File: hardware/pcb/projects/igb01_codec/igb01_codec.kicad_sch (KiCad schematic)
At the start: 46 parts, among them J1 Conn_01x08, J2 Conn_01x08, U1 AK4619

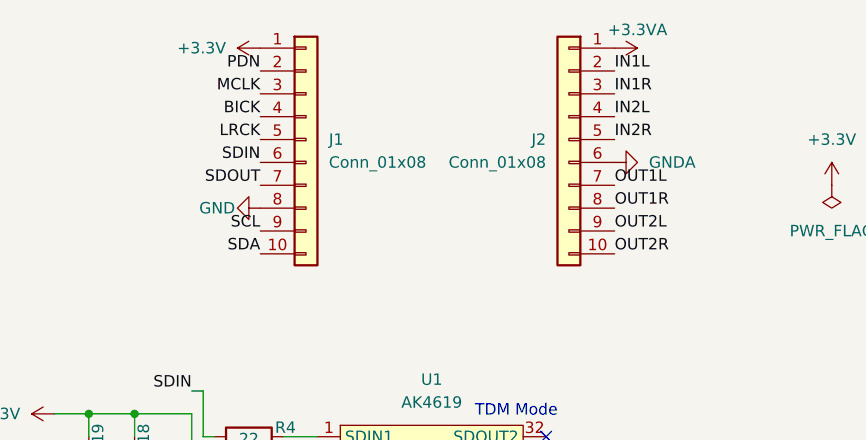
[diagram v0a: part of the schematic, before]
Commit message: add control pcb schematic
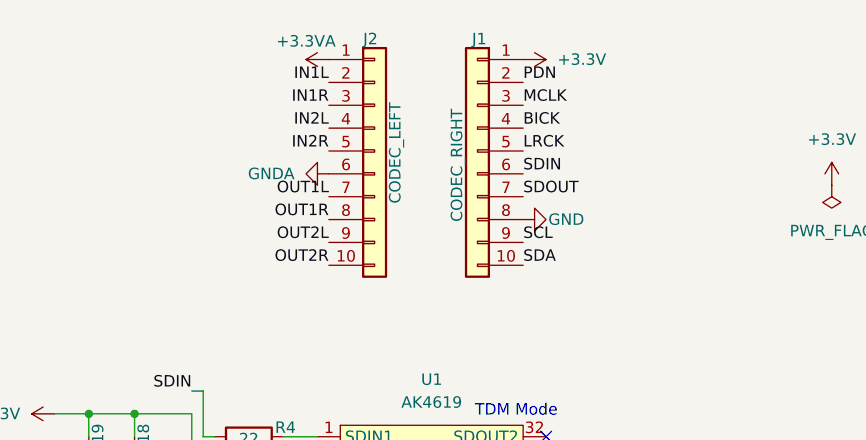
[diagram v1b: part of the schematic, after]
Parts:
- J1: value Conn_01x08 -> CODEC_RIGHT
- J2: value Conn_01x08 -> CODEC_LEFT
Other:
- moved on the sheet: J1, J2
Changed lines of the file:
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@@
 	)
 	(label "SDOUT"
-		(at 124.46 39.37 180)
+		(at 153.67 40.64 0)
 		(effects
 			(font
 				(size 1.27 1.27)
 			)
-			(justify right bottom)
+			(justify left bottom)
 		)
 	)
@@
 	)
 	(label "IN1L"
-		(at 163.83 26.67 0)
+		(at 132.08 27.94 180)
 		(effects
 			(font
 				(size 1.27 1.27)
 			)
-			(justify left bottom)
+			(justify right bottom)
 		)
 	)
@@
 	)
 	(label "OUT1R"
-		(at 163.83 41.91 0)
+		(at 132.08 43.18 180)
 		(effects
 			(font
 				(size 1.27 1.27)
 			)
-			(justify left bottom)
+			(justify right bottom)
 		)
 	)
 	(label "OUT2R"
-		(at 163.83 46.99 0)
+		(at 132.08 48.26 180)
 		(effects
 			(font
 				(size 1.27 1.27)
 			)
-			(justify left bottom)
+			(justify right bottom)
 		)
 	)
 	(label "OUT2L"
-		(at 163.83 44.45 0)
+		(at 132.08 45.72 180)
 		(effects
 			(font
 				(size 1.27 1.27)
 			)
-			(justify left bottom)
+			(justify right bottom)
 		)
 	)
@@
 	)
 	(label "LRCK"
-		(at 124.46 34.29 180)
+		(at 153.67 35.56 0)
 		(effects
 			(font
 				(size 1.27 1.27)
 			)
-			(justify right bottom)
+			(justify left bottom)
 		)
 	)
 	(label "OUT1L"
-		(at 163.83 39.37 0)
+		(at 132.08 40.64 180)
 		(effects
 			(font
 				(size 1.27 1.27)
 			)
-			(justify left bottom)
+			(justify right bottom)
 		)
 	)
@@
 	)
 	(label "SDA"
-		(at 124.46 46.99 180)
+		(at 153.67 48.26 0)
 		(effects
 			(font
 				(size 1.27 1.27)
 			)
-			(justify right bottom)
+			(justify left bottom)
 		)
 	)
 	(label "IN1R"
-		(at 163.83 29.21 0)
+		(at 132.08 30.48 180)
 		(effects
 			(font
 				(size 1.27 1.27)
 			)
-			(justify left bottom)
+			(justify right bottom)
 		)
 	)
 	(label "SDIN"
-		(at 124.46 36.83 180)
+		(at 153.67 38.1 0)
 		(effects
 			(font
 				(size 1.27 1.27)
 			)
-			(justify right bottom)
+			(justify left bottom)
 		)
 	)
 	(label "BICK"
-		(at 124.46 31.75 180)
+		(at 153.67 33.02 0)
 		(effects
 			(font
 				(size 1.27 1.27)
 			)
-			(justify right bottom)
+			(justify left bottom)
 		)
 	)
@@
 	)
 	(label "MCLK"
-		(at 124.46 29.21 180)
+		(at 153.67 30.48 0)
 		(effects
 			(font
 				(size 1.27 1.27)
 			)
-			(justify right bottom)
+			(justify left bottom)
 		)
 	)
@@
 	)
 	(label "IN2L"
-		(at 163.83 31.75 0)
+		(at 132.08 33.02 180)
 		(effects
 			(font
 				(size 1.27 1.27)
 			)
-			(justify left bottom)
+			(justify right bottom)
 		)
 	)
@@
 	)
 	(label "PDN"
-		(at 124.46 26.67 180)
+		(at 153.67 27.94 0)
 		(effects
 			(font
 				(size 1.27 1.27)
 			)
-			(justify right bottom)
+			(justify left bottom)
 		)
 	)
 	(label "IN2R"
-		(at 163.83 34.29 0)
+		(at 132.08 35.56 180)
 		(effects
 			(font
 				(size 1.27 1.27)
 			)
-			(justify left bottom)
+			(justify right bottom)
 		)
 	)
 	(label "SCL"
-		(at 124.46 44.45 180)
+		(at 153.67 45.72 0)
 		(effects
 			(font
 				(size 1.27 1.27)
 			)
-			(justify right bottom)
+			(justify left bottom)
 		)
 	)
@@
 	(symbol
 		(lib_id "power:GNDA")
-		(at 163.83 36.83 90)
+		(at 132.08 38.1 270)
+		(mirror x)
 		(unit 1)
 		(exclude_from_sim no)
@@
 		(fields_autoplaced yes)
 		(property "Reference" "#PWR019"
-			(at 170.18 36.83 0)
+			(at 125.73 38.1 0)
 			(effects
 				(font
@@
 		)
 		(property "Value" "GNDA"
-			(at 167.64 36.8299 90)
+			(at 128.27 38.0999 90)
 			(effects
 				(font
@@
 		)
 		(property "Footprint" ""
-			(at 163.83 36.83 0)
+			(at 132.08 38.1 0)
 			(effects
 				(font
@@
 		)
 		(property "Datasheet" ""
-			(at 163.83 36.83 0)
+			(at 132.08 38.1 0)
 			(effects
 				(font
@@
 		)
 		(property "Description" "Power symbol creates a global label with name \"GNDA\" , analog ground"
-			(at 163.83 36.83 0)
+			(at 132.08 38.1 0)
 			(effects
 				(font
@@
 	(symbol
 		(lib_id "Connector_Generic:Conn_01x10")
-		(at 158.75 34.29 0)
-		(mirror y)
+		(at 137.16 35.56 0)
 		(unit 1)
 		(exclude_from_sim no)
@@
 		(dnp no)
 		(property "Reference" "J2"
-			(at 156.21 34.2899 0)
+			(at 135.89 23.114 0)
 			(effects
 				(font
@@
 			)
 		)
-		(property "Value" "Conn_01x08"
-			(at 156.21 36.8299 0)
+		(property "Value" "CODEC_LEFT"
+			(at 139.446 41.402 90)
 			(effects
 				(font
@@
 		)
 		(property "Footprint" ""
-			(at 158.75 34.29 0)
+			(at 137.16 35.56 0)
 			(effects
 				(font
@@
 		)
 		(property "Datasheet" "~"
-			(at 158.75 34.29 0)
+			(at 137.16 35.56 0)
 			(effects
 				(font
@@
 		)
 		(property "Description" "Generic connector, single row, 01x10, script generated (kicad-library-utils/schlib/autogen/connector/)"
-			(at 158.75 34.29 0)
+			(at 137.16 35.56 0)
 			(effects
 				(font
@@
 	(symbol
 		(lib_id "power:+3.3V")
-		(at 124.46 24.13 90)
+		(at 153.67 25.4 270)
+		(mirror x)
 		(unit 1)
 		(exclude_from_sim no)
@@
 		(fields_autoplaced yes)
 		(property "Reference" "#PWR016"
-			(at 128.27 24.13 0)
+			(at 149.86 25.4 0)
 			(effects
 				(font
@@
 		)
 		(property "Value" "+3.3V"
-			(at 120.65 24.1299 90)
+			(at 157.48 25.3999 90)
 			(effects
 				(font
@@
 		)
 		(property "Footprint" ""
-			(at 124.46 24.13 0)
+			(at 153.67 25.4 0)
 			(effects
 				(font
@@
 		)
 		(property "Datasheet" ""
-			(at 124.46 24.13 0)
+			(at 153.67 25.4 0)
 			(effects
 				(font
@@
 		)
 		(property "Description" "Power symbol creates a global label with name \"+3.3V\""
-			(at 124.46 24.13 0)
+			(at 153.67 25.4 0)
 			(effects
 				(font
@@
 	(symbol
 		(lib_id "power:GND")
-		(at 124.46 41.91 270)
+		(at 153.67 43.18 90)
+		(mirror x)
 		(unit 1)
 		(exclude_from_sim no)
@@
 		(dnp no)
 		(property "Reference" "#PWR017"
-			(at 118.11 41.91 0)
+			(at 160.02 43.18 0)
 			(effects
 				(font
@@
 		)
 		(property "Value" "GND"
-			(at 121.666 41.91 90)
+			(at 156.464 43.18 90)
 			(effects
 				(font
@@
 		)
 		(property "Footprint" ""
-			(at 124.46 41.91 0)
+			(at 153.67 43.18 0)
 			(effects
 				(font
@@
 		)
 		(property "Datasheet" ""
-			(at 124.46 41.91 0)
+			(at 153.67 43.18 0)
 			(effects
 				(font
@@
 		)
 		(property "Description" "Power symbol creates a global label with name \"GND\" , ground"
-			(at 124.46 41.91 0)
+			(at 153.67 43.18 0)
 			(effects
 				(font
@@
 	(symbol
 		(lib_id "Connector_Generic:Conn_01x10")
-		(at 129.54 34.29 0)
+		(at 148.59 35.56 0)
+		(mirror y)
 		(unit 1)
 		(exclude_from_sim no)
@@
 		(on_board yes)
 		(dnp no)
-		(fields_autoplaced yes)
 		(property "Reference" "J1"
-			(at 132.08 34.2899 0)
+			(at 149.606 23.114 0)
 			(effects
 				(font
@@
 			)
 		)
-		(property "Value" "Conn_01x08"
-			(at 132.08 36.8299 0)
+		(property "Value" "CODEC_RIGHT"
+			(at 146.304 43.434 90)
 			(effects
 				(font
@@
 		)
 		(property "Footprint" ""
-			(at 129.54 34.29 0)
+			(at 148.59 35.56 0)
 			(effects
 				(font
@@
 		)
 		(property "Datasheet" "~"
-			(at 129.54 34.29 0)
+			(at 148.59 35.56 0)
 			(effects
 				(font
@@
 		)
 		(property "Description" "Generic connector, single row, 01x10, script generated (kicad-library-utils/schlib/autogen/connector/)"
-			(at 129.54 34.29 0)
+			(at 148.59 35.56 0)
 			(effects
 				(font
@@
 	(symbol
 		(lib_id "power:+3.3VA")
-		(at 163.83 24.13 270)
+		(at 132.08 25.4 90)
+		(mirror x)
 		(unit 1)
 		(exclude_from_sim no)
@@
 		(dnp no)
 		(property "Reference" "#PWR018"
-			(at 160.02 24.13 0)
+			(at 135.89 25.4 0)
 			(effects
 				(font
@@
 		)
 		(property "Value" "+3.3VA"
-			(at 163.068 22.098 90)
+			(at 132.842 23.368 90)
 			(effects
 				(font
@@
 		)
 		(property "Footprint" ""
-			(at 163.83 24.13 0)
+			(at 132.08 25.4 0)
 			(effects
 				(font
@@
 		)
 		(property "Datasheet" ""
-			(at 163.83 24.13 0)
+			(at 132.08 25.4 0)
 			(effects
 				(font
@@
 		)
 		(property "Description" "Power symbol creates a global label with name \"+3.3VA\""
-			(at 163.83 24.13 0)
+			(at 132.08 25.4 0)
 			(effects
 				(font

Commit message: update codec sch&pcb
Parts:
- removed C10, C12, C14, C16: 1u_DIP, symbol Device:C_Small
- removed C11, C13, C15, C9: 1u_SMD, symbol Device:C_Small
- removed JP1: SolderJumper_2_Open, symbol Jumper:SolderJumper_2_Open
- C1, C3, C5, C7: footprint (none) -> Capacitor_SMD:C_1206_3216Metric
- C10: renamed from C18; footprint (none) -> Capacitor_SMD:C_0402_1005Metric
- C11: renamed from C17; footprint (none) -> Capacitor_SMD:C_0603_1608Metric
- C12: renamed from C31; footprint (none) -> Capacitor_SMD:C_0402_1005Metric
- C13: renamed from C32; footprint (none) -> Capacitor_SMD:C_0805_2012Metric
- C14: renamed from C30; footprint (none) -> Capacitor_SMD:C_0603_1608Metric
- C15: renamed from C28; footprint (none) -> Capacitor_SMD:C_0402_1005Metric
- C16: renamed from C29; footprint (none) -> Capacitor_SMD:C_0805_2012Metric
- C17: renamed from C20; footprint (none) -> Capacitor_SMD:C_1206_3216Metric
- C18: renamed from C21; footprint (none) -> Capacitor_THT:C_Rect_L7.2mm_W4.5mm_P5.00mm_FKS2_FKP2_MKS2_MKP2
- C19: renamed from C22; footprint (none) -> Capacitor_SMD:C_1206_3216Metric
- C2, C4, C6, C8: footprint (none) -> Capacitor_THT:C_Rect_L7.2mm_W4.5mm_P5.00mm_FKS2_FKP2_MKS2_MKP2
- C20: renamed from C23; footprint (none) -> Capacitor_THT:C_Rect_L7.2mm_W4.5mm_P5.00mm_FKS2_FKP2_MKS2_MKP2
- C21: renamed from C24; footprint (none) -> Capacitor_SMD:C_1206_3216Metric
- C22: renamed from C25; footprint (none) -> Capacitor_THT:C_Rect_L7.2mm_W4.5mm_P5.00mm_FKS2_FKP2_MKS2_MKP2
- C23: renamed from C26; footprint (none) -> Capacitor_SMD:C_1206_3216Metric
- C24: renamed from C27; footprint (none) -> Capacitor_THT:C_Rect_L7.2mm_W4.5mm_P5.00mm_FKS2_FKP2_MKS2_MKP2
- C9: renamed from C19; footprint (none) -> Capacitor_SMD:C_0805_2012Metric
- J1: renamed from J2; footprint (none) -> Connector_PinHeader_2.54mm:PinHeader_1x10_P2.54mm_Vertical
- J2: renamed from J1; footprint (none) -> Connector_PinHeader_2.54mm:PinHeader_1x10_P2.54mm_Vertical
- R1, R2, R3, R4, R5, R6: footprint (none) -> Resistor_SMD:R_0402_1005Metric
- R10: renamed from R9; footprint (none) -> Resistor_SMD:R_0402_1005Metric
- R7: renamed from R8; footprint (none) -> Resistor_SMD:R_0402_1005Metric
- R8: renamed from R10; footprint (none) -> Resistor_SMD:R_0402_1005Metric
- R9: renamed from R7; footprint (none) -> Resistor_SMD:R_0402_1005Metric
- U1: footprint (none) -> Package_DFN_QFN:QFN-32-1EP_5x5mm_P0.5mm_EP3.6x3.6mm
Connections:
- net GNDA: no longer C1.1, C2.1, C5.1, C6.1
- net IN1L: now also C7.1, C8.1
- net IN1R: now also C5.1, C6.1
- net IN2L: now also C3.1, C4.1; no longer C7.1, C8.1
- net IN2R: now also C1.1, C2.1; no longer C3.1, C4.1
- net at C3.2, C4.2: now also U1.12 (IN3P); no longer U1.10 (IN4P)
- net at C7.2, C8.2: now also U1.16 (IN1P); no longer U1.12 (IN3P)
- net at C5.2, C6.2: now also U1.14 (IN2P); no longer U1.11 (IN3N)
- net at C1.2, C2.2: now also U1.10 (IN4P); no longer U1.9 (IN4N)
- no-connect marks 2 -> 6
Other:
- note added: "Single-Ended Input"
- note removed: "Pseudo-differencial Input"

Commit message: update codec sch&pcb
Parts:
- removed R10, R9: 10k, Resistor_SMD:R_0402_1005Metric, symbol Device:R
- added JP1: Jumper_2_Open, Jumper:SolderJumper-2_P1.3mm_Open_RoundedPad1.0x1.5mm, symbol Jumper:Jumper_2_Open
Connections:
- net BICK: now also J2.3 (Pin_3); no longer J2.4 (Pin_4)
- net GND: now also J2.7 (Pin_7), U1.27 (I2CAD/CS), JP1.2 (B); no longer J2.8 (Pin_8), U1.33 (EP)
- net GNDA: now also U1.33 (EP), JP1.1 (A)
- net LRCK: now also J2.4 (Pin_4); no longer J2.5 (Pin_5)
- net MCLK: now also J2.2 (Pin_2); no longer J2.3 (Pin_3)
- net PDN: now also J2.10 (Pin_10); no longer J2.2 (Pin_2)
- net SDA: now also J2.8 (Pin_8); no longer J2.10 (Pin_10)
- net SDIN: now also J2.5 (Pin_5); no longer J2.6 (Pin_6)
- net SDOUT: now also J2.6 (Pin_6); no longer J2.7 (Pin_7)
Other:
- note removed: "I2C Address"

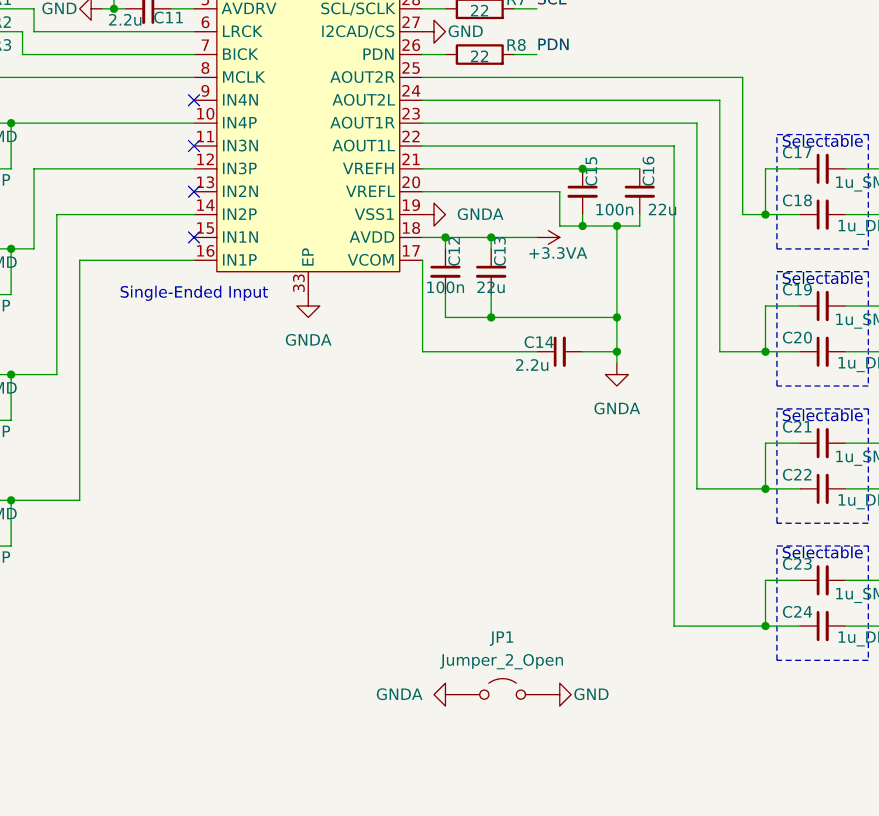
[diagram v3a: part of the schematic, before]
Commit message: update core board sch&pcb
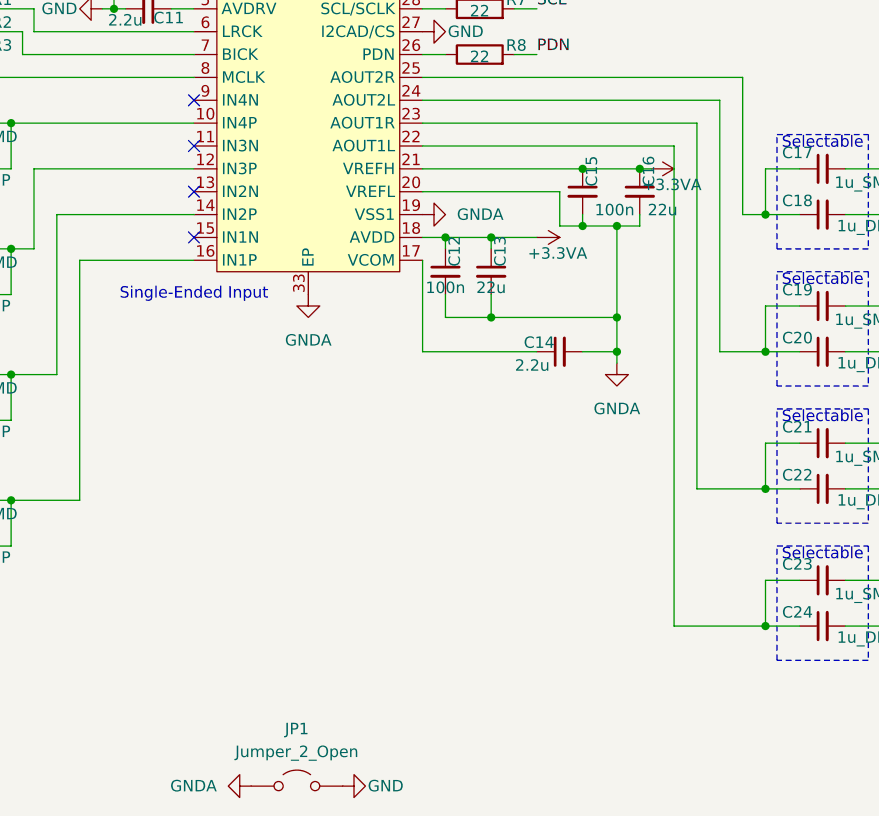
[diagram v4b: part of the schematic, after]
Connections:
- net +3.3VA: now also C15.1, C16.1, U1.21 (VREFH)
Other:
- moved on the sheet: JP1
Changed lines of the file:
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@@
 	)
 	(junction
+		(at 180.34 95.25)
+		(diameter 0)
+		(color 0 0 0 0)
+	)
+	(junction
 		(at 110.49 90.17)
 		(diameter 0)
@@
 	(wire
 		(pts
+			(xy 180.34 95.25) (xy 181.61 95.25)
+		)
+		(stroke
+			(width 0)
+			(type default)
+		)
+	)
+	(wire
+		(pts
 			(xy 208.28 110.49) (xy 208.28 115.57)
 		)
@@
 	(symbol
 		(lib_id "power:GND")
-		(at 170.18 153.67 90)
+		(at 147.32 163.83 90)
 		(unit 1)
 		(exclude_from_sim no)
@@
 		(dnp no)
 		(property "Reference" "#PWR08"
-			(at 176.53 153.67 0)
+			(at 153.67 163.83 0)
 			(effects
 				(font
@@
 		)
 		(property "Value" "GND"
-			(at 172.974 153.67 90)
+			(at 150.114 163.83 90)
 			(effects
 				(font
@@
 		)
 		(property "Footprint" ""
-			(at 170.18 153.67 0)
+			(at 147.32 163.83 0)
 			(effects
 				(font
@@
 		)
 		(property "Datasheet" ""
-			(at 170.18 153.67 0)
+			(at 147.32 163.83 0)
 			(effects
 				(font
@@
 		)
 		(property "Description" "Power symbol creates a global label with name \"GND\" , ground"
-			(at 170.18 153.67 0)
+			(at 147.32 163.83 0)
 			(effects
 				(font
@@
 	(symbol
 		(lib_id "power:GNDA")
-		(at 160.02 153.67 270)
+		(at 137.16 163.83 270)
 		(unit 1)
 		(exclude_from_sim no)
@@
 		(fields_autoplaced yes)
 		(property "Reference" "#PWR07"
-			(at 153.67 153.67 0)
+			(at 130.81 163.83 0)
 			(effects
 				(font
@@
 		)
 		(property "Value" "GNDA"
-			(at 156.21 153.6699 90)
+			(at 133.35 163.8299 90)
 			(effects
 				(font
@@
 		)
 		(property "Footprint" ""
-			(at 160.02 153.67 0)
+			(at 137.16 163.83 0)
 			(effects
 				(font
@@
 		)
 		(property "Datasheet" ""
-			(at 160.02 153.67 0)
+			(at 137.16 163.83 0)
 			(effects
 				(font
@@
 		)
 		(property "Description" "Power symbol creates a global label with name \"GNDA\" , analog ground"
-			(at 160.02 153.67 0)
+			(at 137.16 163.83 0)
 			(effects
 				(font
@@
 	(symbol
 		(lib_id "Jumper:Jumper_2_Open")
-		(at 165.1 153.67 0)
+		(at 142.24 163.83 0)
 		(unit 1)
 		(exclude_from_sim no)
@@
 		(fields_autoplaced yes)
 		(property "Reference" "JP1"
-			(at 165.1 147.32 0)
+			(at 142.24 157.48 0)
 			(effects
 				(font
@@
 		)
 		(property "Value" "Jumper_2_Open"
-			(at 165.1 149.86 0)
+			(at 142.24 160.02 0)
 			(effects
 				(font
@@
 		)
 		(property "Footprint" "Jumper:SolderJumper-2_P1.3mm_Open_RoundedPad1.0x1.5mm"
-			(at 165.1 153.67 0)
+			(at 142.24 163.83 0)
 			(effects
 				(font
@@
 		)
 		(property "Datasheet" "~"
-			(at 165.1 153.67 0)
+			(at 142.24 163.83 0)
 			(effects
 				(font
@@
 		)
 		(property "Description" "Jumper, 2-pole, open"
-			(at 165.1 153.67 0)
+			(at 142.24 163.83 0)
 			(effects
 				(font
@@
 					(unit 1)
 				)
+			)
+		)
+	)
+	(symbol
+		(lib_id "power:+3.3VA")
+		(at 181.61 95.25 270)
+		(unit 1)
+		(exclude_from_sim no)
+		(in_bom yes)
+		(on_board yes)
+		(dnp no)
+		(property "Reference" "#PWR018"
+			(at 177.8 95.25 0)
+			(effects
+				(font
+					(size 1.27 1.27)
+				)
+				(hide yes)
+			)
+		)
+		(property "Value" "+3.3VA"
+			(at 180.594 97.028 90)
+			(effects
+				(font
+					(size 1.27 1.27)
+				)
+				(justify left)
+			)
+		)
+		(property "Footprint" ""
+			(at 181.61 95.25 0)
+			(effects
+				(font
+					(size 1.27 1.27)
+				)
+				(hide yes)
+			)
+		)
+		(property "Datasheet" ""
+			(at 181.61 95.25 0)
+			(effects
+				(font
+					(size 1.27 1.27)
+				)
+				(hide yes)
+			)
+		)
+		(property "Description" "Power symbol creates a global label with name \"+3.3VA\""
+			(at 181.61 95.25 0)
+			(effects
+				(font
+					(size 1.27 1.27)
+				)
+				(hide yes)
+			)
+		)
+		(pin "1"
+		)
+		(instances
+			(project "igb01_codec"
+				(path "/825b51f3-faae-4f15-b0e8-fb5f4d162927"
+					(reference "#PWR018")
+					(unit 1)
+				)
